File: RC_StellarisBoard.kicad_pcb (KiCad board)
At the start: 2 copper layers, 51 parts, among them K1 CONN_3, K2 CONN_3, K3 CONN_3, K4 CONN_3, K5 CONN_3, P1 CONN_2, P2 CONN_1, P3 CONN_1, P4 CONN_1, P5 CONN_1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

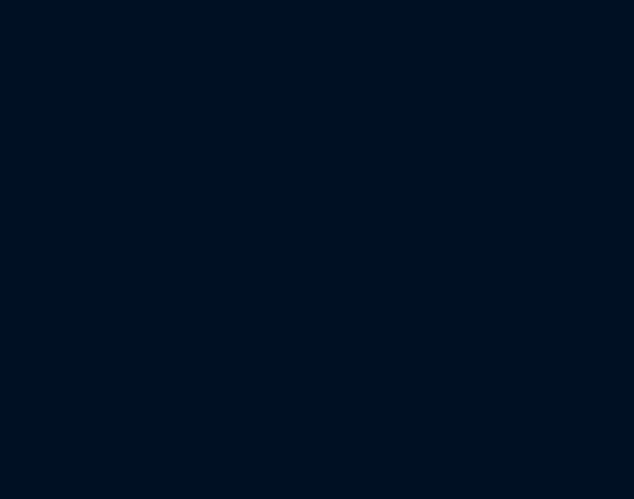
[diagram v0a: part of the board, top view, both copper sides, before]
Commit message: boost, mosfet + shunt + board
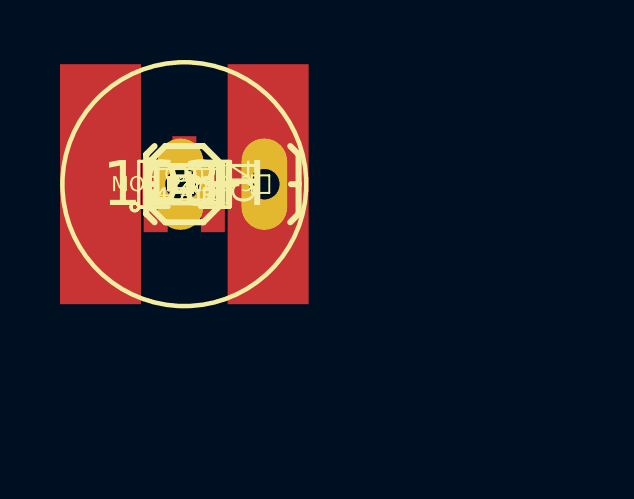
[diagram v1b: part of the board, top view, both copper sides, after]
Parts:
- added C10, C9: 4.7uF, SM0805, F.Cu at (0.00, 0.00)
- added C8: 0.68nF, SM0603, F.Cu at (0.00, 0.00)
- added L3: 10uH, bournes_7.8, F.Cu at (0.00, 0.00)
- added P10: XT-60 out, SparkFun-1X02_LOCK_LONGPADS, F.Cu at (0.00, 0.00)
- added P11: CONN_1, SparkFun-1X01, F.Cu at (0.00, 0.00)
- added Q4: MOS_P_(1-2-3), SOT23, F.Cu at (0.00, 0.00)
- added R20: 120K, SM0603, F.Cu at (0.00, 0.00)
- added R21: 10k, SM0603, F.Cu at (0.00, 0.00)
- added R22: 5k, SM0603, F.Cu at (0.00, 0.00)
- added U4: TPS61170_DRV_6_DRV6_1P6X1, DRV6_1P6X1, F.Cu at (0.00, 0.00)
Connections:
- D1 pad 1: N-0000027 -> N-0000024
- D1 pad 2: +BATT -> +24V
- Q1 pad D: +BATT -> N-000007
- Q1 pad G: N-0000015 -> N-0000022
- Q2 pad G: N-0000032 (its old number) -> /mosfet_on
- R10 pad 1: N-0000032 (its old number) -> /mosfet_on
- R11 pad 1: N-0000015 -> N-0000024
- R19 pad 1: /Battery_out -> +BATT
- R19 pad 2: N-0000018 -> N-000007
- R9 pad 1: N-0000015 -> N-0000022
- U1 pad 3: N-0000037 -> (no net)
- U1 pad 4: N-0000036 -> (no net)
- U1 pad 7: N-0000035 (its old number) -> (no net)
- U1 pad 8: N-0000034 (its old number) -> (no net)
- U3 pad 6: N-0000017 -> (no net)

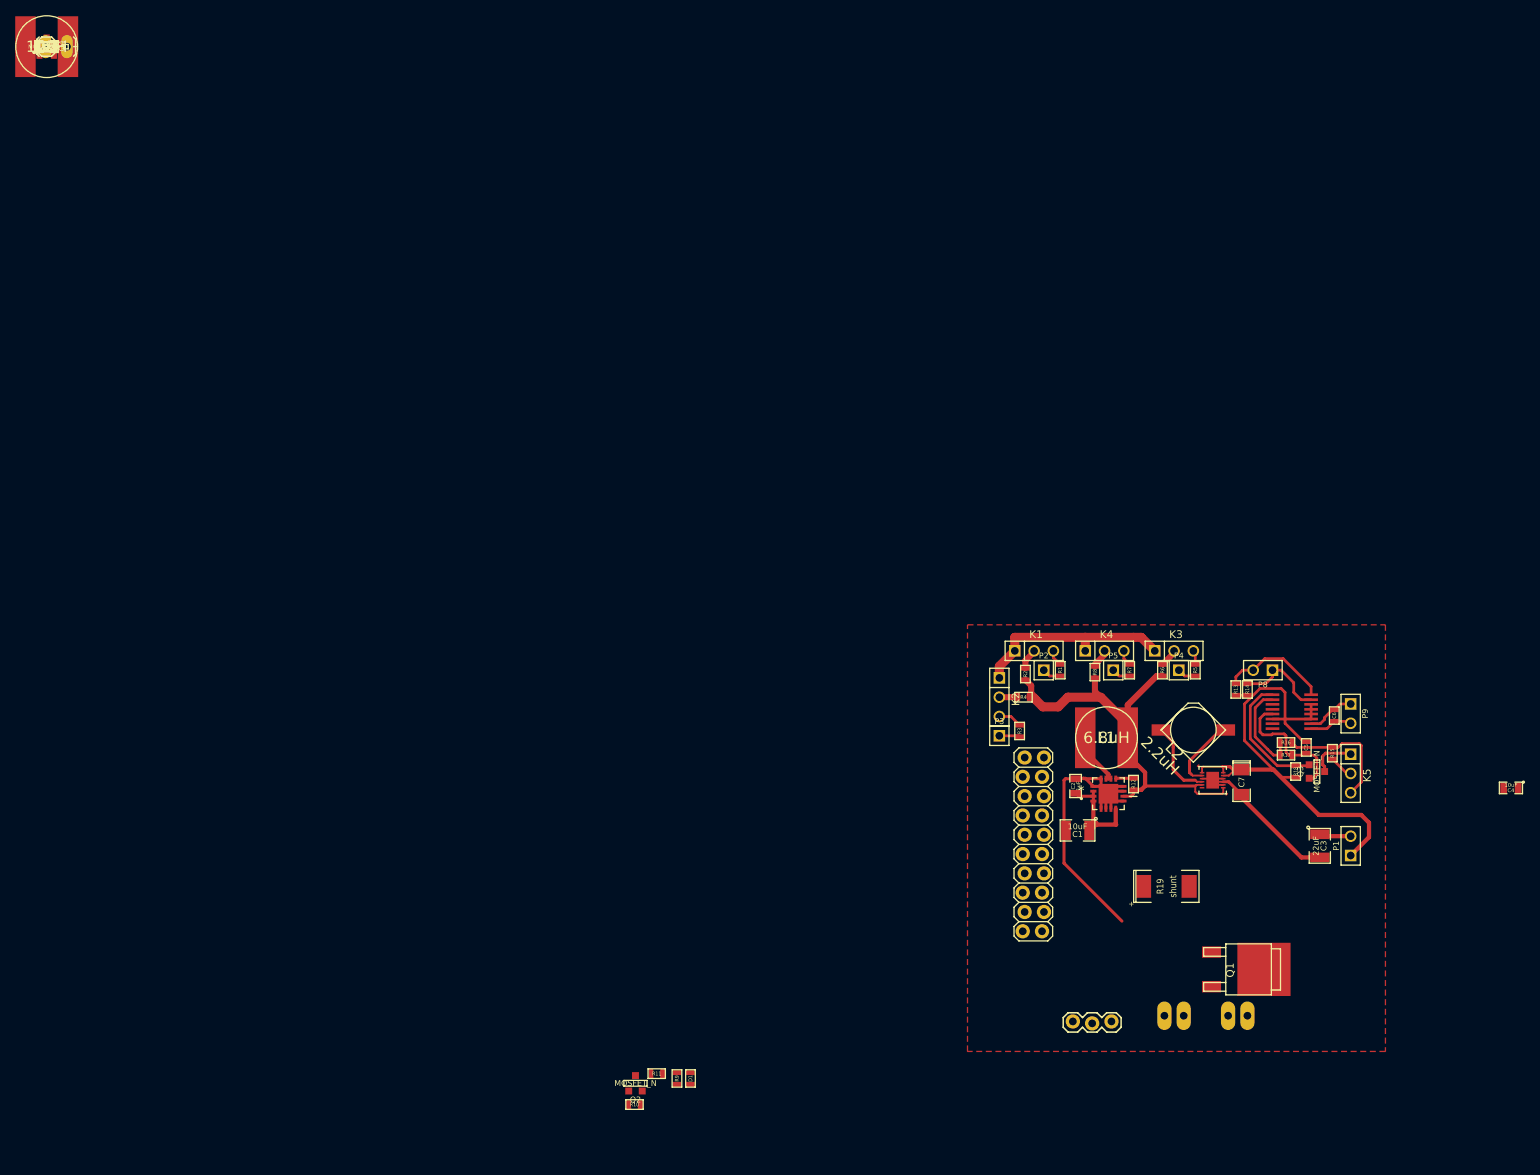
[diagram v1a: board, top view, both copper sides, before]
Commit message: falta footprints diodo
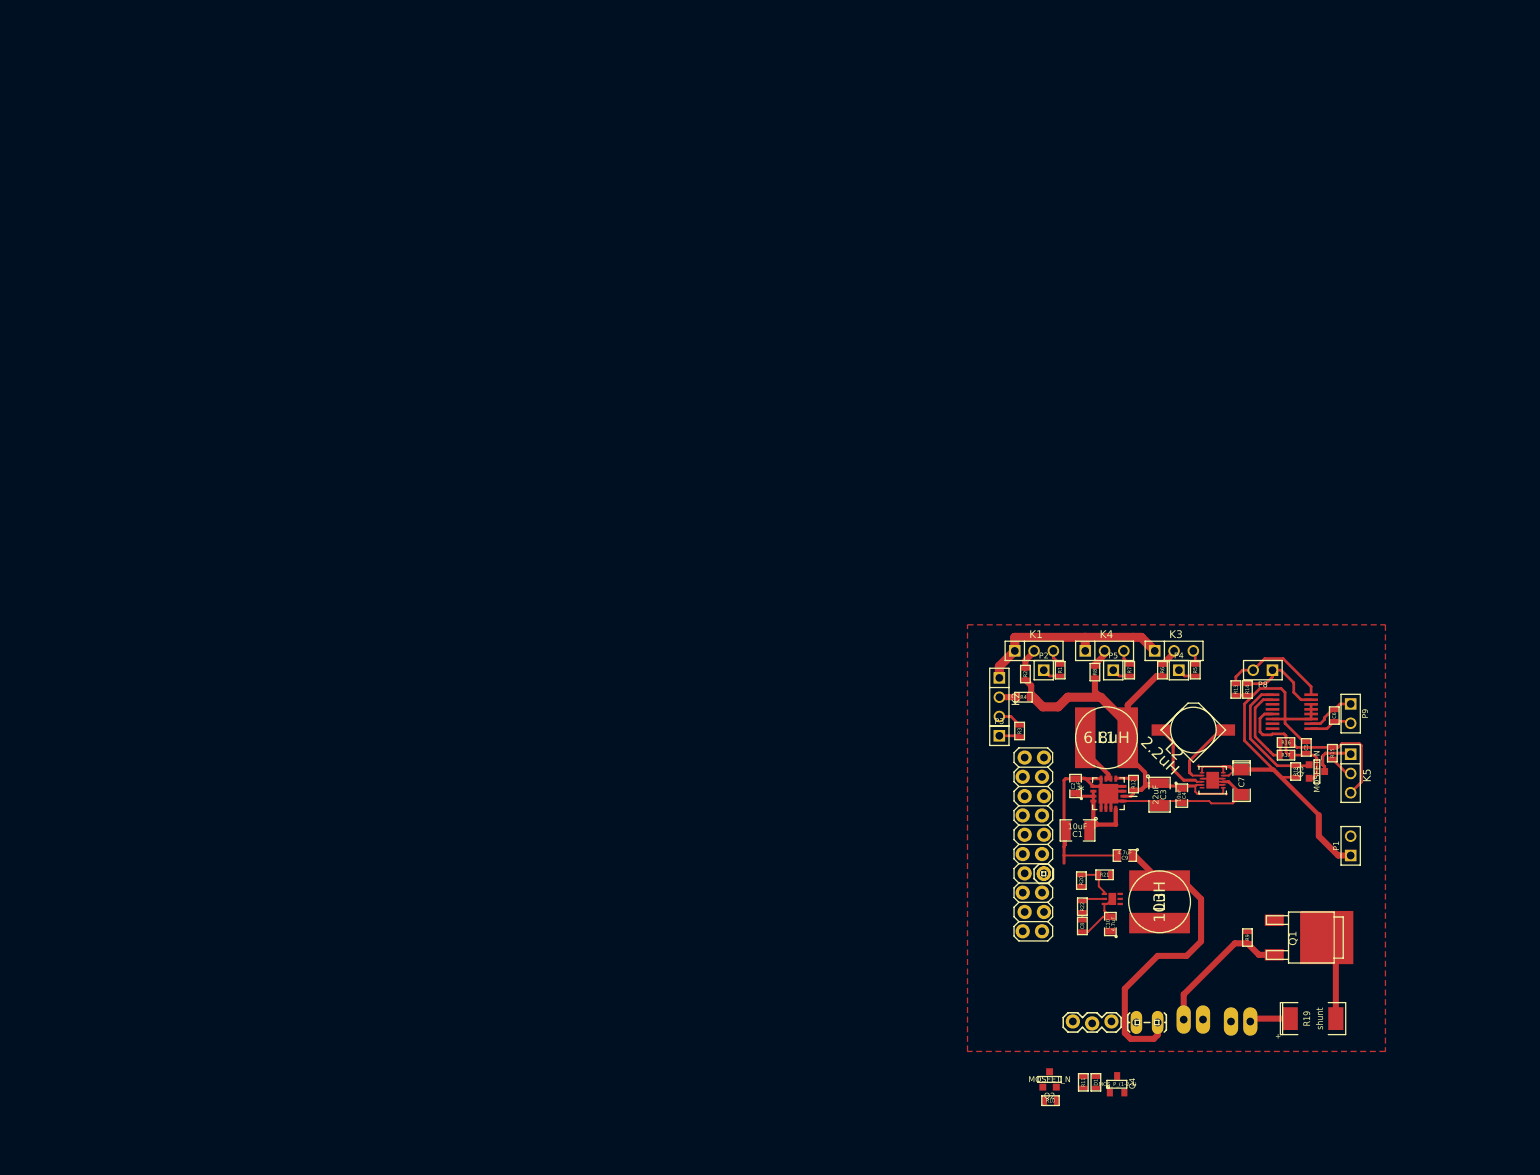
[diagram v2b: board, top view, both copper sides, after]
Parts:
- moved Q4 196.2 mm to (140.8, 136.5)
- moved P10 192.6 mm to (143.5, 128.4)
- moved L3 184.7 mm to (146.4, 112.5), turned to 90 degrees
- moved C10 181.4 mm to (140.0, 115.4), turned to 90 degrees
- moved U4 179.5 mm to (140.2, 112.1)
- moved C8 178.8 mm to (136.3, 115.7), turned to 270 degrees
- moved C9 177.3 mm to (141.9, 106.4), turned to 180 degrees
- moved R22 177.1 mm to (136.3, 113.2), turned to 90 degrees
- moved R21 176.8 mm to (139.2, 109.0), turned to 180 degrees
- moved R20 174.9 mm to (136.1, 109.7), turned to 90 degrees
- moved P11 170.5 mm to (131.2, 108.8)
- moved R9 77.3 mm to (158.0, 117.2), turned to 270 degrees
- moved R11 56.1 mm to (136.4, 136.3), turned to 90 degrees
- moved R10 54.7 mm to (132.1, 138.7)
- moved Q2 54.5 mm to (132.0, 135.9)
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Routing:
- net /Battery_boost: track 0.00 -> 42.0 mm
- net /Battery_out: track 3.20 -> 21.8 mm
- net GND: track 115.5 -> 129.1 mm
- net N-000007: track 0.00 -> 11.2 mm
- net +BATT: track 13.6 -> 19.0 mm
- net N-0000026: track 0.00 -> 5.11 mm
- net +3.3V: track 71.0 -> 66.7 mm
- net N-0000025: track 0.00 -> 3.00 mm
- net +5V: track 62.7 -> 61.6 mm
- net N-0000027: track 0.00 -> 1.02 mm
- net PE0: track 0.86 -> 0.00 mm
- net /mosfet_on: track 0.00 -> 0.86 mm

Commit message: versao com tudo
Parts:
- removed JP8: CCP, 1X03_LOCK
- added C11: 0.1uF, SM0603, F.Cu at (157.5, 105.4)
- added C12: 0.1uF, SM0603, F.Cu at (162.1, 111.3)
- added D2: DIODESCH, SMB, F.Cu at (145.7, 111.6)
- added P12: CONN_1, SparkFun-1X01, F.Cu at (128.7, 108.8)
- added R23: 3k3, SM0603, F.Cu at (161.5, 101.1)
- added R24: 10k, SM0603, F.Cu at (162.1, 109.7)
- added R25: 10k, SM0603, F.Cu at (164.6, 110.2)
- added U5: INA226, MSOP10-0.5, F.Cu at (161.5, 105.4)
- D1: footprint SM0603 -> SOD123_mod
- L3: footprint bournes_7.8 -> 4x4
- Q4: footprint SOT23 -> SOT23GDS
- moved R11 32.9 mm to (157.6, 111.1), turned to 180 degrees
- moved Q2 31.3 mm to (154.4, 114.0)
- moved D1 29.7 mm to (153.9, 111.1), turned to 180 degrees
- moved Q4 28.3 mm to (158.0, 114.0)
- moved U$3 21.6 mm to (108.2, 104.9)
- moved R10 7.75 mm to (124.5, 137.3)
- moved R20 6.38 mm to (140.6, 114.3), turned to 180 degrees
- moved R21 4.99 mm to (137.9, 113.8), turned to 0 degrees
- moved L3 4.49 mm to (145.8, 108.1)
- moved U4 4.44 mm to (141.2, 107.8)
- moved C8 4.44 mm to (137.3, 111.4)
- moved R22 4.44 mm to (137.3, 108.8)
- moved C10 4.44 mm to (141.0, 111.1)
- moved C9 1.53 mm to (141.2, 105.0)
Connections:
- C1 pad 1: +BATT -> /Battery_out
- C2 pad 1: +BATT -> /Battery_out
- D1 pad 1: N-0000024 (its old number) -> N-0000017
- Q1 pad D: N-000007 -> /V-
- Q1 pad G: N-0000022 (its old number) -> N-000007
- R11 pad 1: N-0000024 (its old number) -> N-0000017
- R19 pad 2: N-000007 -> /V-
- R9 pad 1: N-0000022 (its old number) -> N-000007
- U1 pad 3: (no net) -> N-0000035
- U1 pad 4: (no net) -> N-0000034
- U1 pad 7: (no net) -> N-0000033
- U1 pad 8: (no net) -> N-0000032
- U2 pad 2: +BATT -> /Battery_out
- U2 pad 3: +BATT -> /Battery_out
- U2 pad 4: +BATT -> /Battery_out
- U2 pad 8: +BATT -> /Battery_out
- U3 pad 6: (no net) -> N-000006
- U4 pad 5: (no net) -> N-0000023
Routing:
- net /mosfet_on: track 0.86 -> 70.2 mm
- net /ina_alert: track 0.00 -> 62.4 mm
- net GND: track 129.1 -> 180.8 mm
- net /SCL: track 14.4 -> 64.3 mm
- net /SDA: track 12.0 -> 59.3 mm
- net /V-: track 0.00 -> 21.9 mm
- net +3.3V: track 66.7 -> 85.1 mm
- net /Battery_out: track 21.8 -> 35.4 mm
- net +24V: track 0.00 -> 11.0 mm
- net N-0000017: track 0.00 -> 11.0 mm
- net N-0000012: track 5.11 -> 14.0 mm
- net N-0000024: track 0.00 -> 8.62 mm
- net +BATT: track 19.0 -> 27.5 mm
- net N-0000013: track 0.00 -> 6.26 mm
- net N-000007: track 11.2 -> 4.98 mm
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
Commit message: v1 completa
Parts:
- removed P1: CONN_2, PIN_ARRAY_2X1
- removed P8: I2C, PIN_ARRAY_2X1
- removed U$3: M10X22X10_LOCK, 2X10_LOCK
- added K6: CONN_3, SparkFun-1X03_LOCK, F.Cu at (158.8, 82.0)
- added R26: ina0, SM0603, F.Cu at (157.4, 102.5)
- added R27: ina0, SM0603, F.Cu at (161.4, 99.1)
- K1, K2, K3, K4, K5: footprint PIN_ARRAY_3X1 -> SparkFun-1X03_LOCK
- P2, P3, P4, P5: footprint PIN_ARRAY_1 -> SparkFun-1X01
- P9: footprint PIN_ARRAY_2X1 -> SparkFun-1X02_LOCK
- moved R10 34.8 mm to (151.9, 115.8), turned to 270 degrees
- moved P10 22.0 mm to (148.2, 106.9), turned to 180 degrees
- moved R23 5.93 mm to (157.5, 105.4), turned to 90 degrees
- moved U4 5.08 mm to (141.2, 112.9)
- moved C10 5.08 mm to (141.0, 116.2)
- moved C8 5.08 mm to (137.3, 116.5)
- moved C9 5.08 mm to (141.2, 110.1)
- moved D2 5.08 mm to (145.7, 116.7)
- moved L3 5.08 mm to (145.8, 113.2)
- moved R20 5.08 mm to (140.6, 119.4)
- moved R21 5.08 mm to (137.9, 118.9)
- moved R22 5.08 mm to (137.3, 113.9)
- moved R19 4.19 mm to (167.6, 123.8)
- moved K4 2.67 mm to (136.5, 79.5)
- moved K3 2.54 mm to (145.8, 79.4)
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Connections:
- P12 pad 1: /ina_alert -> N-0000014
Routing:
- net /Battery_out: track 35.4 -> 98.9 mm, vias 0 -> 3
- net /ina_alert: track 62.4 -> 8.60 mm
- net GND: track 180.8 -> 225.4 mm, vias 0 -> 2
- net /mosfet_on: track 70.2 -> 33.2 mm, vias 0 -> 2
- net /Battery_boost: track 45.6 -> 10.1 mm
- net N-0000014: track 0.00 -> 34.4 mm, vias 0 -> 2
- net +24V: track 11.0 -> 43.9 mm
- net +BATT: track 27.5 -> 37.8 mm
- net /V-: track 21.9 -> 12.4 mm
- net (no net): track 0.36 -> 3.85 mm
- net +3.3V: track 85.1 -> 87.8 mm
- net /SCL: track 64.3 -> 65.5 mm
- added copper zone on F.Cu, net +BATT
- added copper zone on F.Cu, net /Battery_out
- added copper zone on F.Cu, net /V-
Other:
- net class Default: via_dia 0.889 -> 1.589; via_drill 0.635 -> 1

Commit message: pads
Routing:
- net GND: track 225.4 -> 230.9 mm
- net (no net): track 3.85 -> 0.36 mm
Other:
- board outline added: 54.4 x 55.4 mm
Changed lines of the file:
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@@
     (links 145)
     (no_connects 0)
-    (area 0 0 0 0)
+    (area 91.631431 76.11175 182.059917 149.63746)
     (thickness 1.6)
-    (drawings 214)
+    (drawings 220)
     (tracks 545)
     (zones 0)
@@
     )
   )
+  (gr_line (start 122.047 76.8985) (end 122.6185 76.8985) (angle 90) (layer Edge.Cuts) (width 0.15))
+  (gr_line (start 122.047 132.334) (end 122.047 76.8985) (angle 90) (layer Edge.Cuts) (width 0.15))
+  (gr_line (start 176.4665 132.334) (end 122.047 132.334) (angle 90) (layer Edge.Cuts) (width 0.15))
+  (gr_line (start 176.4665 76.8985) (end 176.4665 132.334) (angle 90) (layer Edge.Cuts) (width 0.15))
+  (gr_line (start 176.149 76.8985) (end 176.4665 76.8985) (angle 90) (layer Edge.Cuts) (width 0.15))
+  (gr_line (start 122.6185 76.8985) (end 176.149 76.8985) (angle 90) (layer Edge.Cuts) (width 0.15))
   (dimension 55.118146 (width 0.3) (layer Dwgs.User)
     (gr_text 55,118mm (at 148.496247 148.223963 0.1320176915) (layer Dwgs.User)
@@
     (effects (font (size 0.8128 0.8128) (thickness 0.0635)) (justify right))
   )
-  (segment (start 161.544 105.918) (end 161.798 105.664) (width 0.254) (layer F.Cu) (net 0))
-  (segment (start 163.957 106.172) (end 164.719 106.172) (width 0.254) (layer F.Cu) (net 0))
-  (segment (start 163.449 105.664) (end 163.957 106.172) (width 0.254) (layer F.Cu) (net 0))
-  (segment (start 161.798 105.664) (end 163.449 105.664) (width 0.254) (layer F.Cu) (net 0))
   (segment (start 151.4475 94.6785) (end 151.5745 94.5515) (width 0.254) (layer F.Cu) (net 0))
   (segment (start 155.194 98.425) (end 155.321 98.298) (width 0.254) (layer F.Cu) (net 0))
@@
   (segment (start 153.289 115.062) (end 153.543 115.062) (width 0.36) (layer F.Cu) (net 15))
   (segment (start 131.28244 108.77804) (end 131.21894 108.77804) (width 0.254) (layer F.Cu) (net 15))
+  (segment (start 161.036 106.299) (end 161.036 106.2355) (width 0.254) (layer F.Cu) (net 16))
+  (segment (start 163.957 105.664) (end 165.5445 107.2515) (width 0.254) (layer F.Cu) (net 16))
+  (segment (start 161.6075 105.664) (end 163.957 105.664) (width 0.254) (layer F.Cu) (net 16))
+  (segment (start 161.036 106.2355) (end 161.6075 105.664) (width 0.254) (layer F.Cu) (net 16))
   (segment (start 162.179 99.06) (end 163.703 99.06) (width 0.254) (layer F.Cu) (net 16))
   (segment (start 159.512 99.06) (end 160.655 99.06) (width 0.254) (layer F.Cu) (net 16))
@@
     (connect_pads (clearance 0.508))
     (min_thickness 0.254)
-    (fill (arc_segments 16) (thermal_gap 0.508) (thermal_bridge_width 0.508))
+    (fill (arc_segments 16) (thermal_gap 0.508) (thermal_bridge_width 1.08))
     (polygon
       (pts
@@
     (connect_pads (clearance 0.508))
     (min_thickness 0.254)
-    (fill (arc_segments 16) (thermal_gap 0.508) (thermal_bridge_width 0.508))
+    (fill (arc_segments 16) (thermal_gap 0.508) (thermal_bridge_width 1.508))
     (polygon
       (pts
@@
     (connect_pads (clearance 0.508))
     (min_thickness 0.254)
-    (fill (arc_segments 16) (thermal_gap 0.508) (thermal_bridge_width 0.508))
+    (fill (arc_segments 16) (thermal_gap 0.508) (thermal_bridge_width 1.08))
     (polygon
       (pts

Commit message: added nordic
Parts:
- added P1: CONN_1, SparkFun-1X01, F.Cu at (149.3, 145.1)
- Q1: footprint sot428 -> sot404
- moved R19 3.30 mm to (167.5, 127.1)
- moved Q1 1.83 mm to (166.5, 118.2)
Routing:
- net (no net): track 0.36 -> 9.82 mm
- net /SCL: track 65.5 -> 56.3 mm
- net /SDA: track 59.6 -> 51.4 mm
- net GND: track 230.9 -> 237.2 mm
- net +BATT: track 37.8 -> 40.9 mm

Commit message: v2
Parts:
- added P13: CONN_1, SparkFun-1X01, F.Cu at (128.5, 96.0)
- added P14: CONN_4, SparkFun-1X04-SMD_mod, F.Cu at (130.7, 122.8)
- added P8: CONN_3X2, SparkFun-2X3, F.Cu at (128.5, 111.4)
- P1: value CONN_1 -> CONN_4; footprint SparkFun-1X01 -> SparkFun-1X04-SMD_mod
- moved P1 33.1 mm to (130.7, 117.7), turned to 180 degrees
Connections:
- P1 pad 1: +3.3V -> GND
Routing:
- net +3.3V: track 87.8 -> 134.3 mm
- net /~IRQ: track 0.00 -> 18.5 mm
- net /~CS: track 0.00 -> 16.2 mm
- net /~CE: track 0.00 -> 14.3 mm
- net /MOSI: track 0.00 -> 12.0 mm
- net /SCK: track 0.00 -> 9.49 mm
- net /MISO: track 0.00 -> 6.95 mm
- net GND: track 237.2 -> 243.5 mm

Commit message: v3, n confirmado, added fan diode
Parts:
- added D3: DIODESCH, SMB, F.Cu at (166.5, 102.0)
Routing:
- net GND: track 243.5 -> 275.8 mm
- net /Battery_out: track 98.5 -> 119.2 mm
- net N-000001: track 6.03 -> 14.1 mm
- net (no net): track 9.82 -> 5.85 mm
